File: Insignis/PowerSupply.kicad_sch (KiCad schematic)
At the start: 14 parts, among them IC1 AP3012KTR-G1, IC2 LT8653SEV#PBF

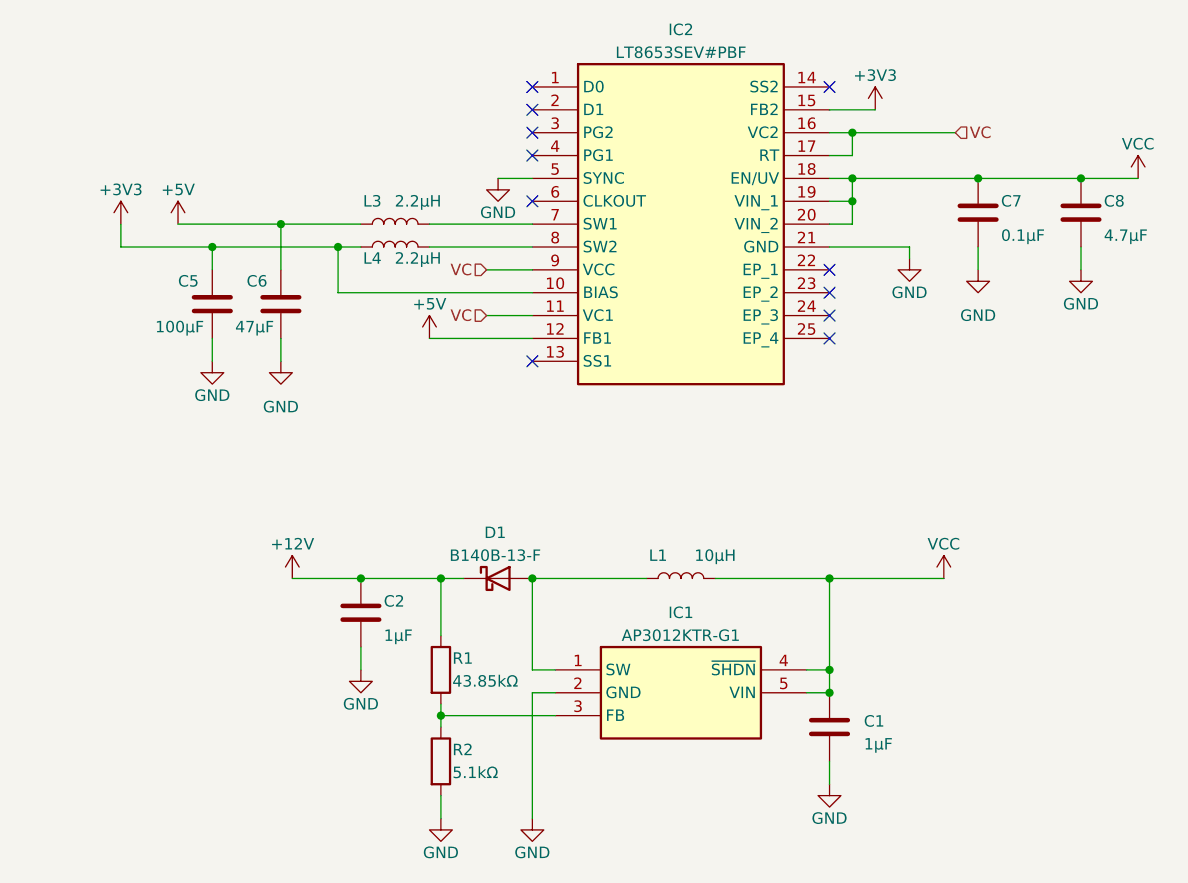
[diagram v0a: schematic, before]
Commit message: Fixed ERC errors
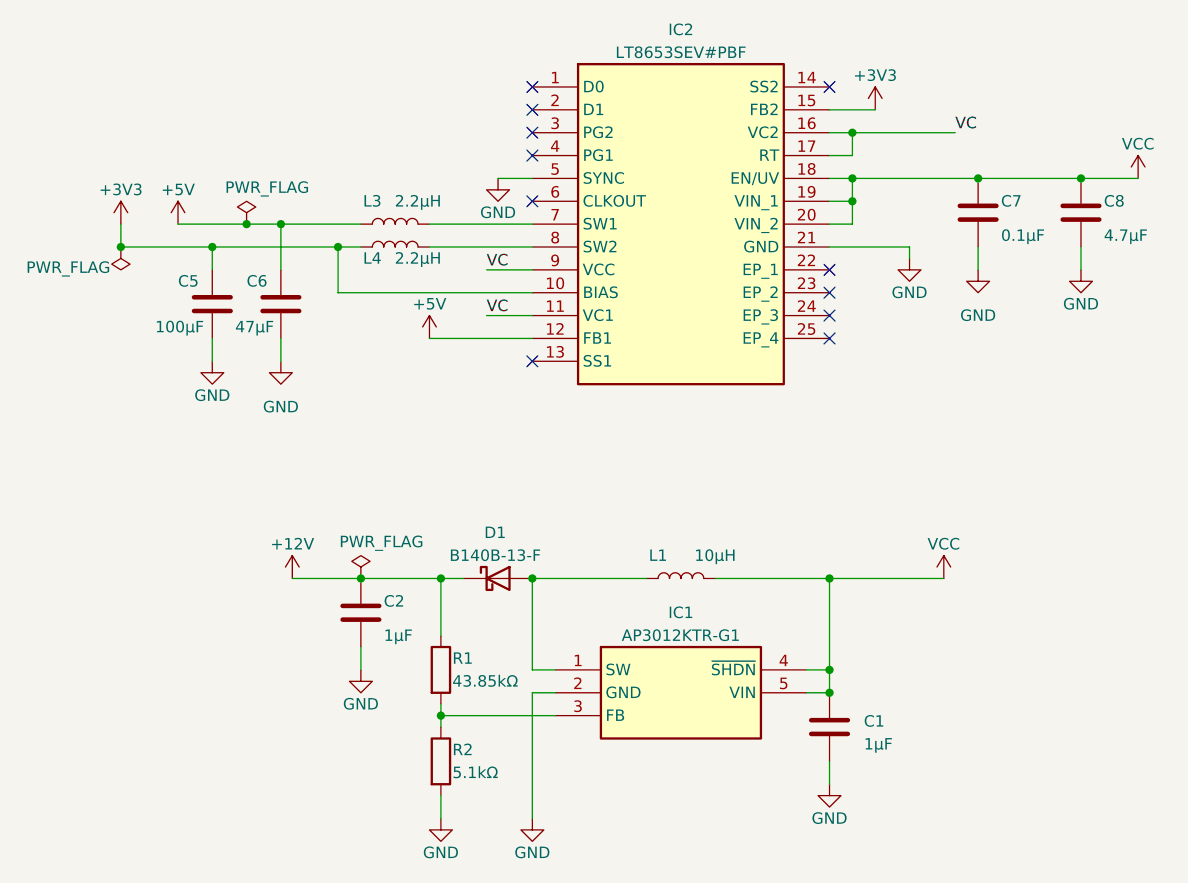
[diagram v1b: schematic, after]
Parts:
- IC1: footprint SOT95P282X145-5N -> AP3012KTR-G1:SOT95P282X145-5N
- IC2: footprint LT8653SEVPBF -> LT8653SEV#PBF:LT8653SEVPBF
